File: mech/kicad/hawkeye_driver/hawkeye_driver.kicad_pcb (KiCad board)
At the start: 2 copper layers, 71.1 x 54.6 mm, 30 parts, among them J1 Conn_02x05_Odd_Even, J2 Screw_Terminal_01x02, Q1 IRLD024, Q2 IRLD024, Q3 IRLD024, U1 74HC595

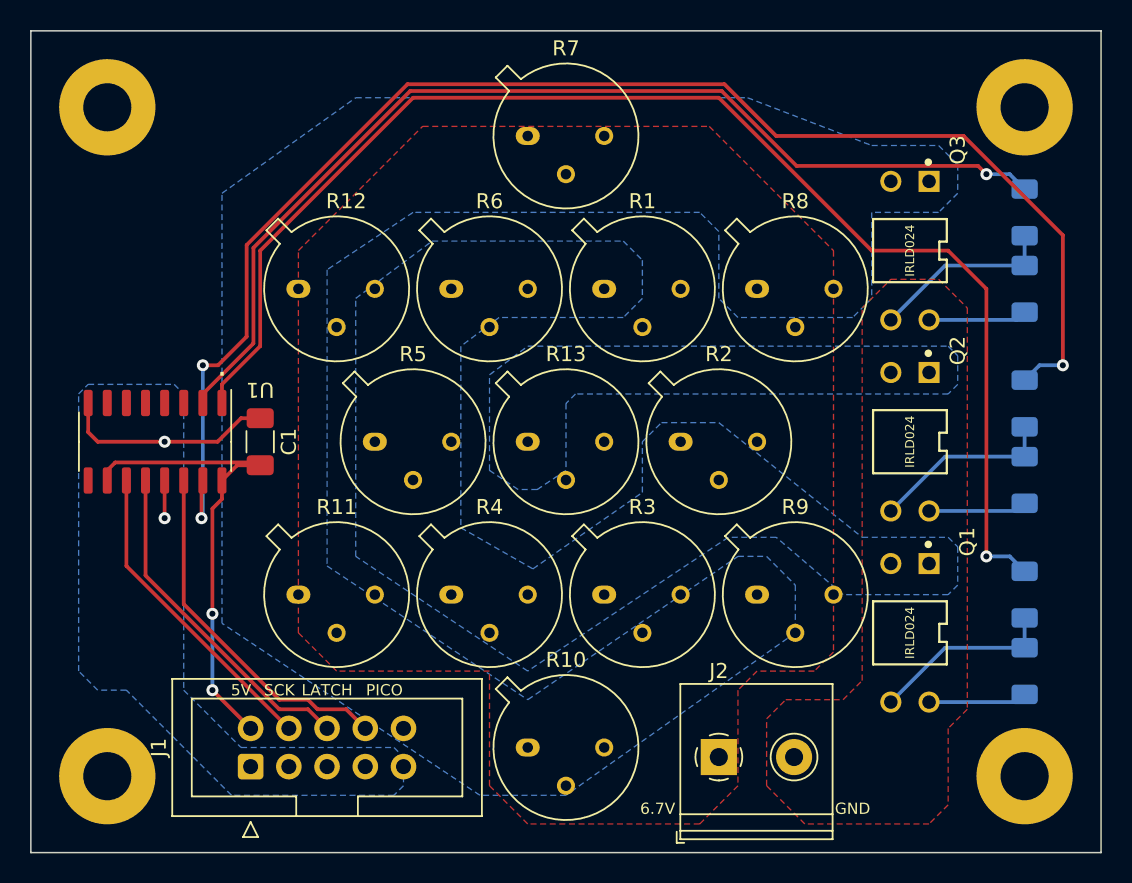
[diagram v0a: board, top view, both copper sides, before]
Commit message: docs updates, pcb updates, photogrammetry updates
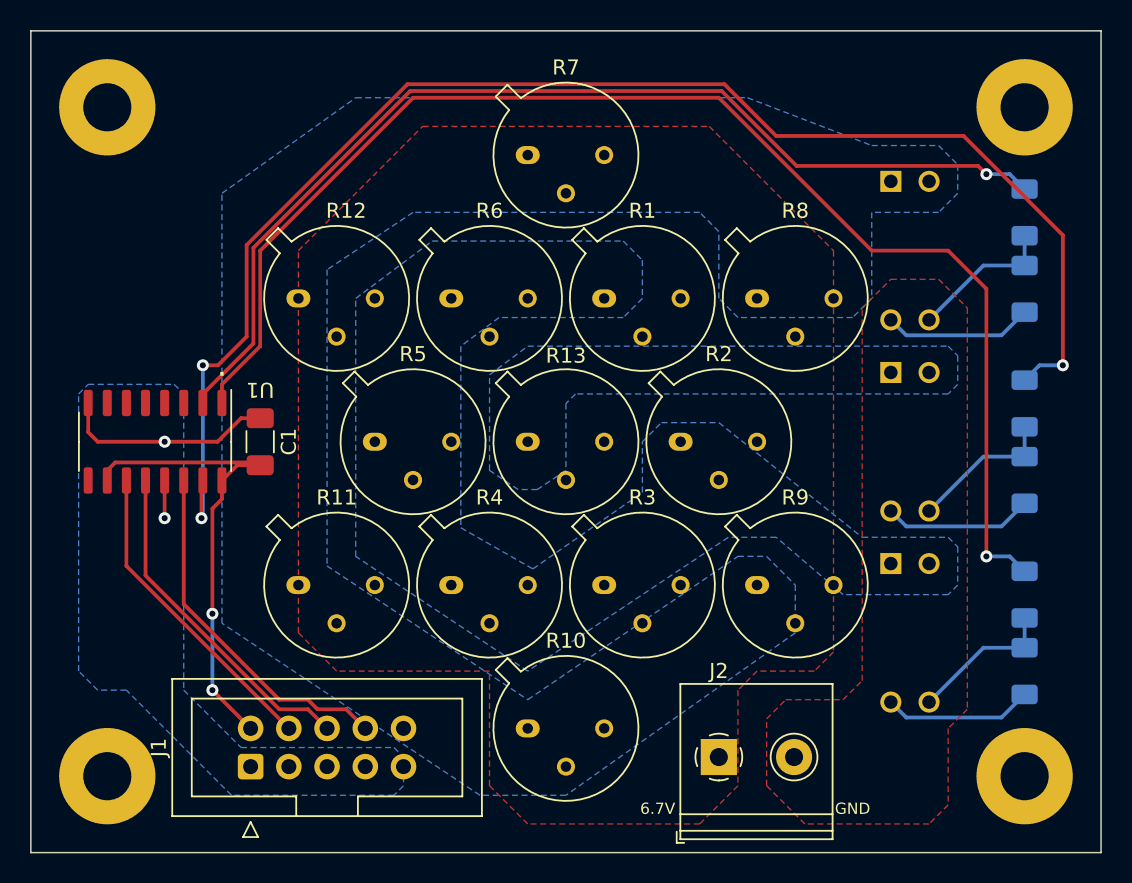
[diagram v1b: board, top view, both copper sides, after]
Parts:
- Q1, Q2, Q3: moved to B.Cu
- moved R10 1.27 mm to (137.2, 110.5)
- moved R7 1.27 mm to (137.2, 72.4)
- moved R1 0.64 mm to (142.2, 81.9)
- moved R12 0.64 mm to (121.9, 81.9)
- moved R6 0.64 mm to (132.1, 81.9)
- moved R8 0.64 mm to (152.4, 81.9)
- moved R11 0.63 mm to (121.9, 101.0)
- moved R3 0.63 mm to (142.2, 101.0)
- moved R4 0.63 mm to (132.1, 101.0)
- moved R9 0.63 mm to (152.4, 101.0)
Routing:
- net GND: track 19.7 -> 29.9 mm
- net Net-(Q1-Pad2): track 12.4 -> 9.83 mm
- net Net-(Q3-Pad2): track 12.4 -> 9.83 mm
- net Net-(Q2-Pad2): track 12.4 -> 9.83 mm
